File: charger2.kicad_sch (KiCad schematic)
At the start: 1 part

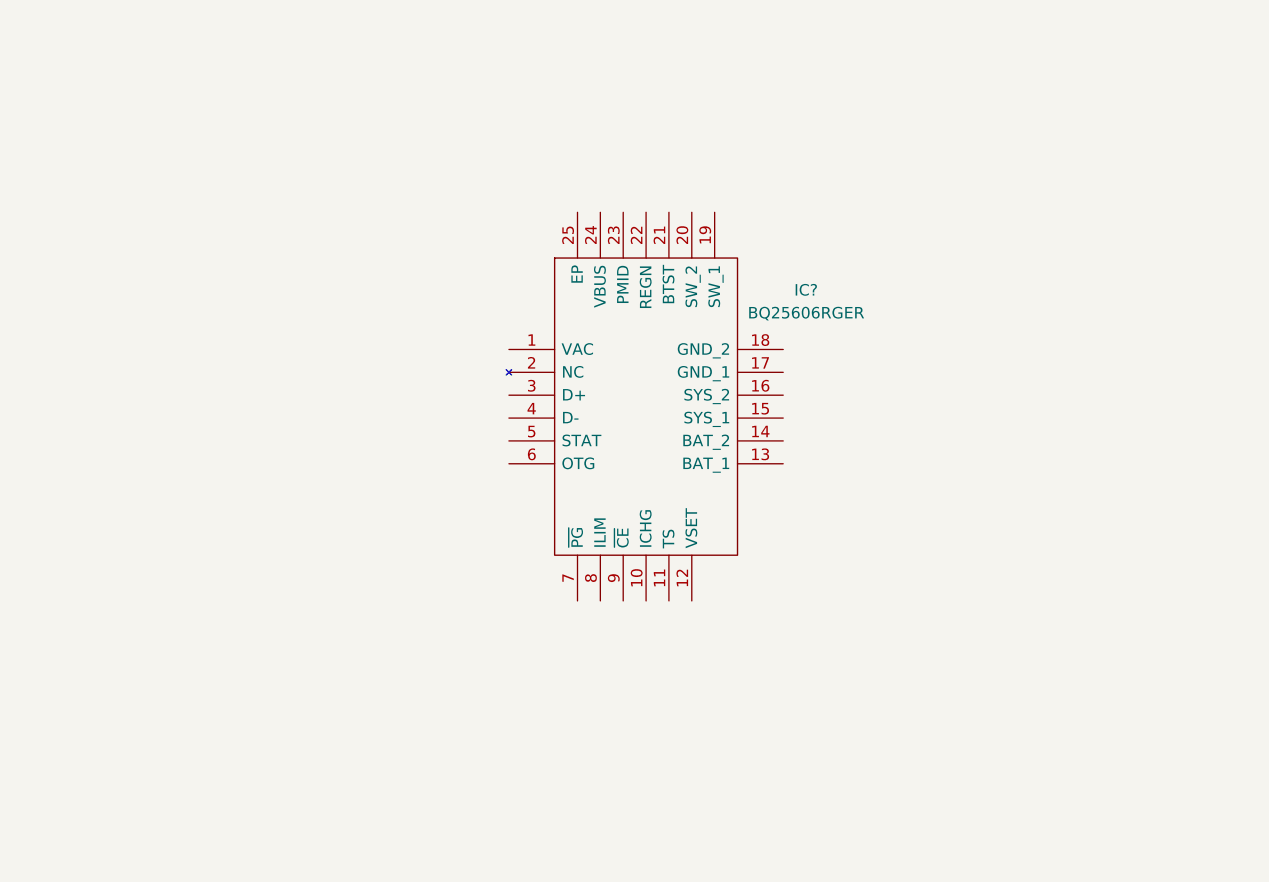
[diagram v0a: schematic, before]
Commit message: Schematic done
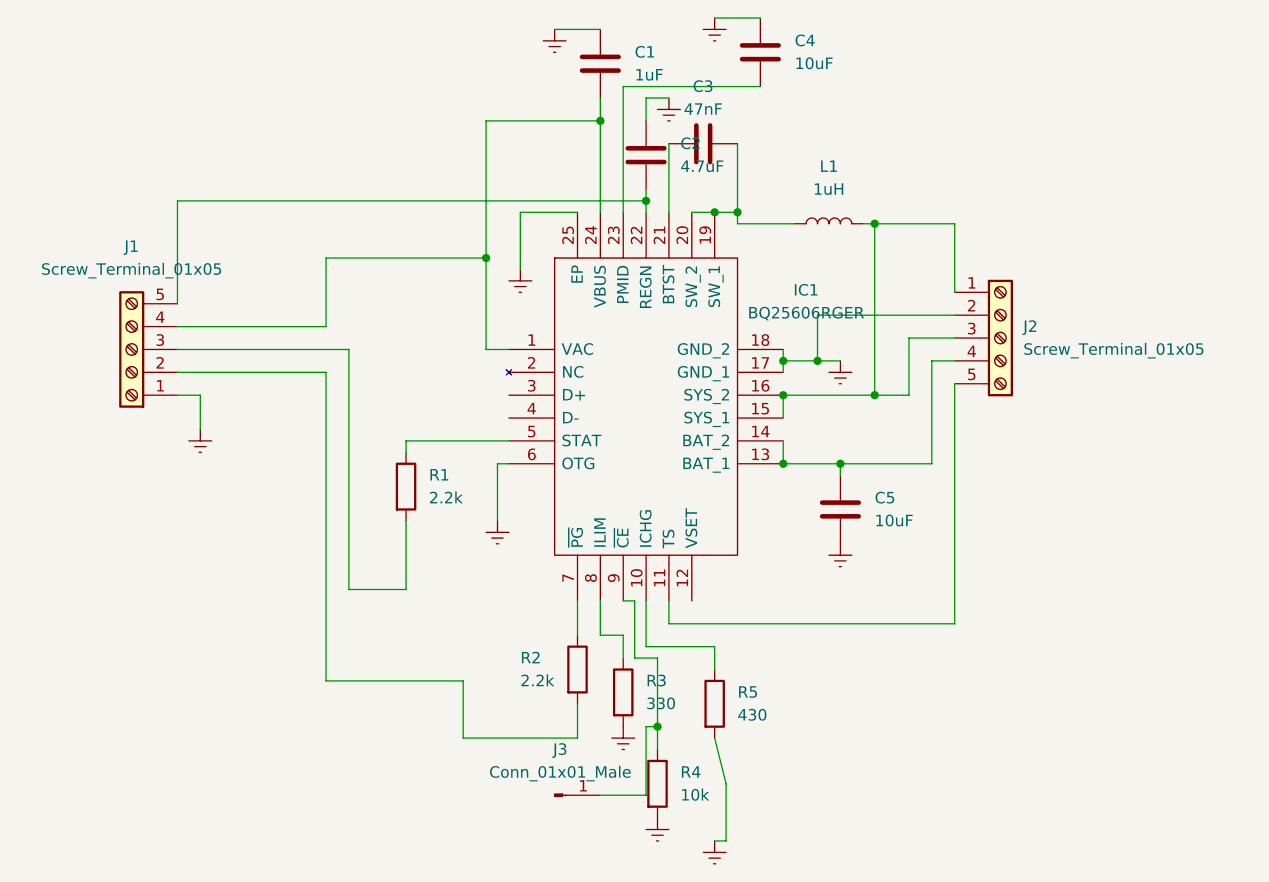
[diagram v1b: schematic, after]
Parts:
- added C1: 1uF, 1uF cap:C1206, symbol Device:C
- added C2: 4.7uF, cap 4.7uf:C1210, symbol Device:C
- added C3: 47nF, 47nF:C1005_Commercial, symbol Device:C
- added C4, C5: 10uF, 10uF MLCC:CAPC2012X94N, symbol Device:C
- added J1, J2: Screw_Terminal_01x05, TerminalBlock_MetzConnect:TerminalBlock_MetzConnect_Type059_RT06305HBWC_1x05_P3.50mm_Horizontal, symbol Connector:Screw_Terminal_01x05
- added J3: Conn_01x01_Male, Connector_PinHeader_1.00mm:PinHeader_1x01_P1.00mm_Vertical, symbol Connector:Conn_01x01_Male
- added L1: 1uH, 1uH indc:IHHP0805ZHER1R0M01, symbol Device:L
- added R1, R2: 2.2k, 2.2k rst:RESC2012X65N, symbol Device:R
- added R3: 330, rst 330:H2C_H2R, symbol Device:R
- added R4: 10k, 10k rst:ERA8KEB1004V, symbol Device:R
- added R5: 430, rst 430:ERJH3, symbol Device:R
- gave numbers to parts that had none: 1
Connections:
- net at IC1.1 (VAC): now also IC1.24 (VBUS), C1.2, J1.4 (Pin_4)
- net at IC1.10 (ICHG): now also R5.1
- net at IC1.11 (TS): now also J2.5 (Pin_5)
- net at IC1.13 (BAT_1): now also IC1.14 (BAT_2), C5.1, J2.4 (Pin_4)
- net at IC1.15 (SYS_1): now also IC1.16 (SYS_2), J2.1 (Pin_1), J2.3 (Pin_3), L1.2
- net Earth: now reaches IC1.17 (GND_1)
- net Earth: now also IC1.18 (GND_2), IC1.25 (EP), IC1.6 (OTG), C1.1, C2.1, C4.1, C5.2, J1.1 (Pin_1), J2.2 (Pin_2), R3.2, R4.2, R5.2
- net at IC1.19 (SW_1): now also IC1.20 (SW_2), C3.2, L1.1
- net at IC1.21 (BTST): now also C3.1
- net at IC1.22 (REGN): now also C2.2, J1.5 (Pin_5)
- net at IC1.23 (PMID): now also C4.2
- net at IC1.5 (STAT): now also R1.1
- net at IC1.7 (~{PG}): now also R2.1
- net at IC1.8 (ILIM): now also R3.1
- net at IC1.9 (~{CE}): now also J3.1 (Pin_1), R4.1
- new net: J1.2 (Pin_2), R2.2
- new net: J1.3 (Pin_3), R1.2
